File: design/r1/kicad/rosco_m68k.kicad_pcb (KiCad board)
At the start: 4 copper layers, 160 x 100 mm, 70 parts, among them IC1 MC68010P10, IC2 ATF16V8QL-15PU, IC3 7493N, IC4 MC68901P, IC5 ATF16V8QL-15PU, IC6 74174N, IC7 7404N, IC8 555N, IC9 74LS01N, Q1 1.8432MHz, Q2 8MHz, U1 AT28C64B-15PU, U2 AT28C64B-15PU, U3 AS6C4008-55PCN, U4 AS6C4008-55PCN

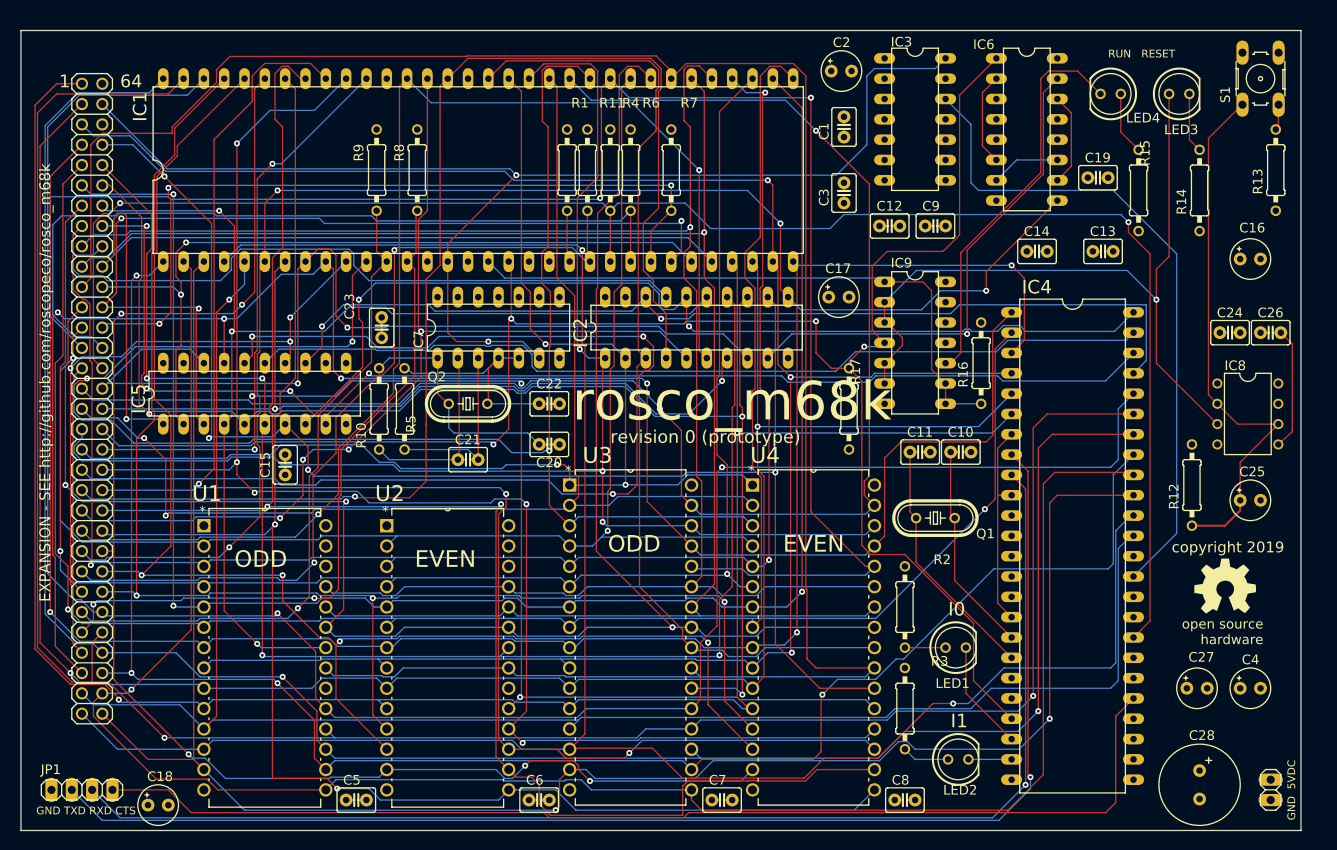
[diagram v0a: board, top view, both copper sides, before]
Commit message: Initial work on r1 board, make ERC and DRC pass
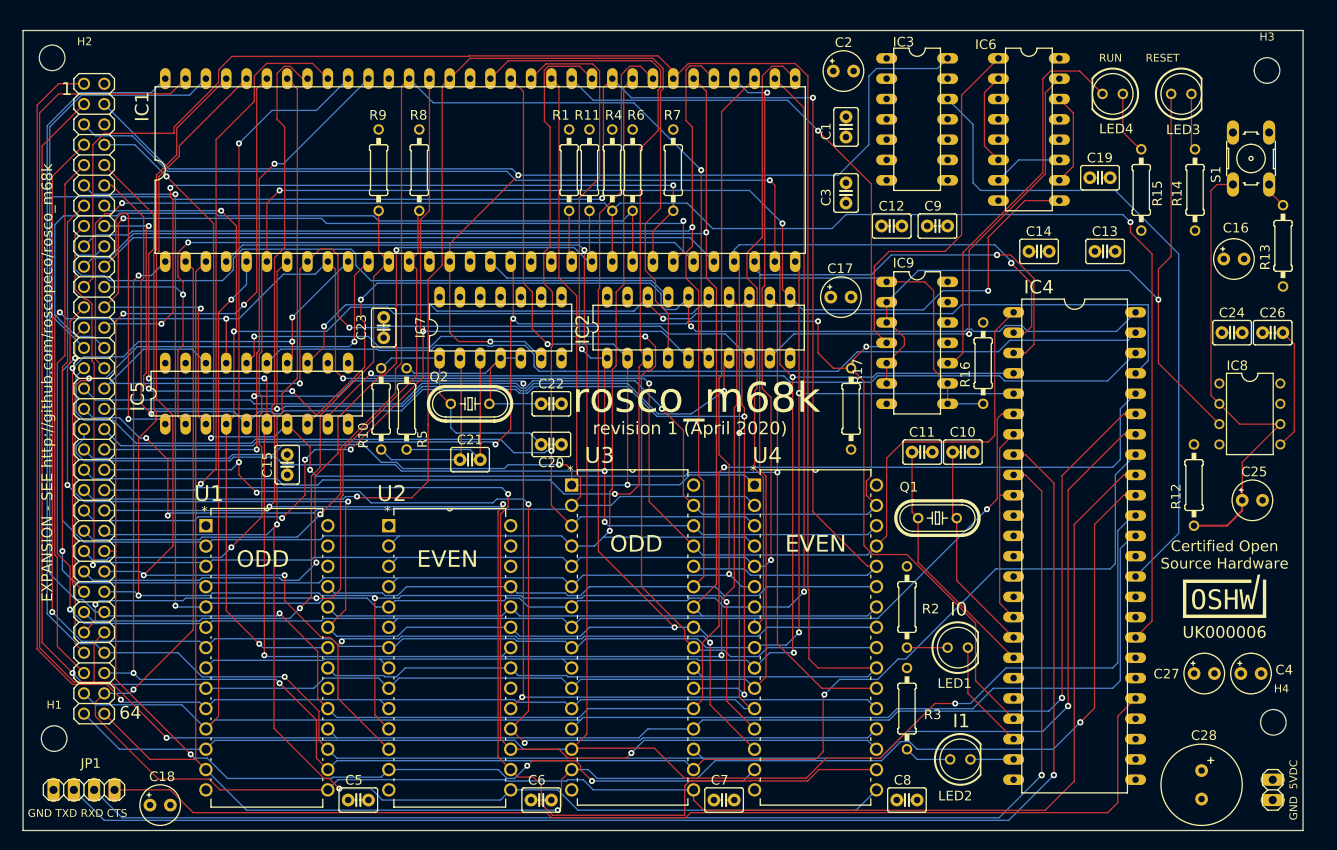
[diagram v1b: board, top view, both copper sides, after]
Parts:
- removed U$1: , rosco_m68k:OSHW_8MM
- added H1: MountingHole, MountingHole:MountingHole_3.2mm_M3, F.Cu at (72.6, 143.5)
- added H2: MountingHole, MountingHole:MountingHole_3.2mm_M3, F.Cu at (72.4, 58.4)
- added H3: MountingHole, MountingHole:MountingHole_3.2mm_M3, F.Cu at (224.3, 60.0)
- added H4: MountingHole, MountingHole:MountingHole_3.2mm_M3, F.Cu at (225.0, 141.5)
- added OSHW_Mono_0.25_Scale: UK000006, rosco_m68k:OSHW_Mono_0.25_Scale, F.Cu at (218.9, 125.7)
- IC2: value ATF16V8QL-15PU -> ATF16V8BQL-15PU
- IC5: value ATF16V8QL-15PU -> ATF16V8BQL
- Q1: value 1.8432MHz -> 3.6864MHz
- moved S1 10.0 mm to (222.3, 71.0)
- moved R13 9.51 mm to (226.3, 81.9)
- moved C16 2.05 mm to (220.1, 83.6)
- moved C27 2.05 mm to (216.4, 135.4)
- moved C4 1.84 mm to (222.2, 135.4)
- moved R14 0.57 mm to (215.3, 74.9)
- moved R15 0.34 mm to (208.5, 74.9)
- moved C11 0.25 mm to (181.2, 107.7)
- moved C12 0.25 mm to (177.3, 79.4)
- moved C17 0.25 mm to (171.0, 88.3)
- moved C2 0.25 mm to (171.3, 60.1)
- moved C26 0.25 mm to (225.0, 92.8)
- moved C6 0.25 mm to (133.5, 151.2)
- moved C8 0.25 mm to (179.2, 151.2)
- moved C9 0.25 mm to (183.1, 79.4)
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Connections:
- net /BOOT renamed BOOT
- net /HALT renamed HALT
- net /IACK renamed IACK
- net /IODTACK renamed IODTACK
- net /MFPDS renamed MFPDS
- net /RAMOE renamed RAMOE
- net R/W renamed RW
- IC4 pad 2: /Cpu_Ram_Rom/A5 -> /Cpu_Ram_Rom/A1
- IC4 pad 3: /Cpu_Ram_Rom/A4 -> /Cpu_Ram_Rom/A2
- IC4 pad 5: /Cpu_Ram_Rom/A2 -> /Cpu_Ram_Rom/A4
- IC4 pad 6: /Cpu_Ram_Rom/A1 -> /Cpu_Ram_Rom/A5
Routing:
- net /Cpu_Ram_Rom/A2: track 251.9 -> 268.2 mm
- net /Cpu_Ram_Rom/A1: track 263.7 -> 277.4 mm, vias 2 -> 3
- net /Cpu_Ram_Rom/A4: track 245.1 -> 232.9 mm
- net Net-(C25-Pad+): track 67.9 -> 58.4 mm
- net /Cpu_Ram_Rom/A5: track 282.9 -> 273.6 mm
- net /Cpu_Ram_Rom/D11: track 190.5 -> 186.9 mm
- net /MC68901_Decoder/UARTTX: track 165.9 -> 169.4 mm
- net /Cpu_Ram_Rom/D5: track 261.5 -> 258.0 mm
- net /Cpu_Ram_Rom/D6: track 273.2 -> 269.9 mm
- net /MC68901_Decoder/UARTRX: track 159.3 -> 161.9 mm
- net AS: track 182.7 -> 185.2 mm
- net /Cpu_Ram_Rom/D2: track 232.4 -> 230.1 mm
- net /Cpu_Ram_Rom/D3: track 239.9 -> 237.6 mm
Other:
- board text added: "Certified Open Source Hardware"
- board text added: "copyright 2020"
- board text added: "revision 1 (April 2020)"
- board text added: "rosco_m68k revision one"
- board text removed: "copyright 2019"
- board text removed: "revision 0 (prototype)"
- board text removed: "rosco_m68k revision zero"

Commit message: Design complete
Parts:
- added J5: GPIO-PANEL, Connector_PinHeader_2.54mm:PinHeader_2x08_P2.54mm_Vertical, F.Cu at (220.9, 146.4)
- added R18: 4K7, rosco_m68k:0207_10, F.Cu at (213.6, 140.4)
- added R19: 4K7, rosco_m68k:0207_10, F.Cu at (213.3, 105.8)
- added REF**: KiCad-Logo2_5mm_SilkScreen, Symbol:KiCad-Logo2_5mm_SilkScreen, B.Cu at (117.0, 70.2)
- moved JP1 154.1 mm to (224.0, 105.9), turned to 270 degrees
- moved JP2 149.4 mm to (75.6, 145.9)
- moved C4 137.6 mm to (84.8, 130.2)
- moved C28 132.8 mm to (83.2, 147.9), turned to 0 degrees
- moved C27 131.7 mm to (84.8, 137.9)
- moved C18 127.9 mm to (213.8, 151.2)
- moved R1 36.9 mm to (148.6, 107.5), turned to 180 degrees
- moved C25 20.0 mm to (215.4, 95.0)
- moved IC8 16.0 mm to (222.5, 86.9)
- moved C16 15.7 mm to (204.4, 82.9)
- moved R8 12.3 mm to (106.0, 72.4)
- moved C24 11.1 mm to (214.1, 83.4), turned to 90 degrees
- moved R11 10.7 mm to (128.8, 72.5)
- moved H4 10.0 mm to (224.3, 151.5)
- moved R9 9.97 mm to (103.2, 72.4)
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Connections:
- IC1 pad 19: Net-(IC1-Pad19) -> VMA
- IC1 pad 20: Net-(IC1-Pad20) -> E
- IC1 pad 21: Net-(IC1-Pad21) -> VPA
- IC4 pad 13: Net-(IC4-Pad13) -> TAO
- IC4 pad 14: Net-(IC4-Pad14) -> TBO
- IC4 pad 19: GND -> TAI
- IC4 pad 20: GND -> TBI
- IC4 pad 24: Net-(IC4-Pad24) -> GPIO1
- IC4 pad 25: Net-(IC4-Pad25) -> GPIO2
- IC4 pad 26: Net-(IC4-Pad26) -> GPIO3
- IC4 pad 27: Net-(IC4-Pad27) -> GPIO4
- IC4 pad 28: Net-(IC4-Pad28) -> GPIO5
- IC4 pad 33: Net-(IC4-Pad33) -> IEO
- JP3 pad 10: EVENROMSEL -> E
- JP3 pad 12: ODDRAMSEL -> VMA
- JP3 pad 14: ODDROMSEL -> IEO
- JP3 pad 8: EVENRAMSEL -> VPA
- R1 pad 1: Net-(IC1-Pad21) -> VCC
- R1 pad 2: VCC -> VPA
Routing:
- net IEO: track 0.00 -> 185.9 mm, vias 0 -> 4
- net /MC68901_Decoder/UARTTX: track 169.4 -> 38.7 mm, vias 1 -> 0
- net /MC68901_Decoder/UARTRX: track 161.9 -> 37.5 mm, vias 1 -> 0
- net EXPSEL: track 86.4 -> 210.3 mm, vias 0 -> 1
- net VPA: track 0.00 -> 103.4 mm, vias 0 -> 3
- net Net-(IC4-Pad29): track 141.6 -> 45.1 mm, vias 0 -> 1
- net ODDROMSEL: track 142.6 -> 237.2 mm
- net EVENROMSEL: track 183.6 -> 277.2 mm, vias 4 -> 7
- net E: track 0.00 -> 71.6 mm, vias 0 -> 2
- net VMA: track 0.00 -> 68.8 mm, vias 0 -> 2
- net TBI: track 0.00 -> 56.8 mm
- net IOSEL: track 173.6 -> 227.2 mm, vias 5 -> 6
- net TAO: track 0.00 -> 40.5 mm
- net TBO: track 0.00 -> 35.7 mm
- net TAI: track 0.00 -> 35.6 mm
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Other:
- outline, holes or cut-outs redrawn
- board text added: "15"
- board text added: "2"
- board text added: "5VDC GND"
- board text added: "63"
- board text added: "CTS RXD TXD GND"
- board text added: "IO & PANEL"
- board text removed: "GND 5VDC"
- board text removed: "GND TXD RXD CTS"
